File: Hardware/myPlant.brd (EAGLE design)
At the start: 141.4 x 16.8 mm, 42 parts, among them IC2 LMV358, Q2 MMBT2222A, SW1 KMR2, SW2 KMR2, U1 FSA3357, U2 NCP1402, U3 ALS-PT19, U6 SI7021, X1 ESP-12

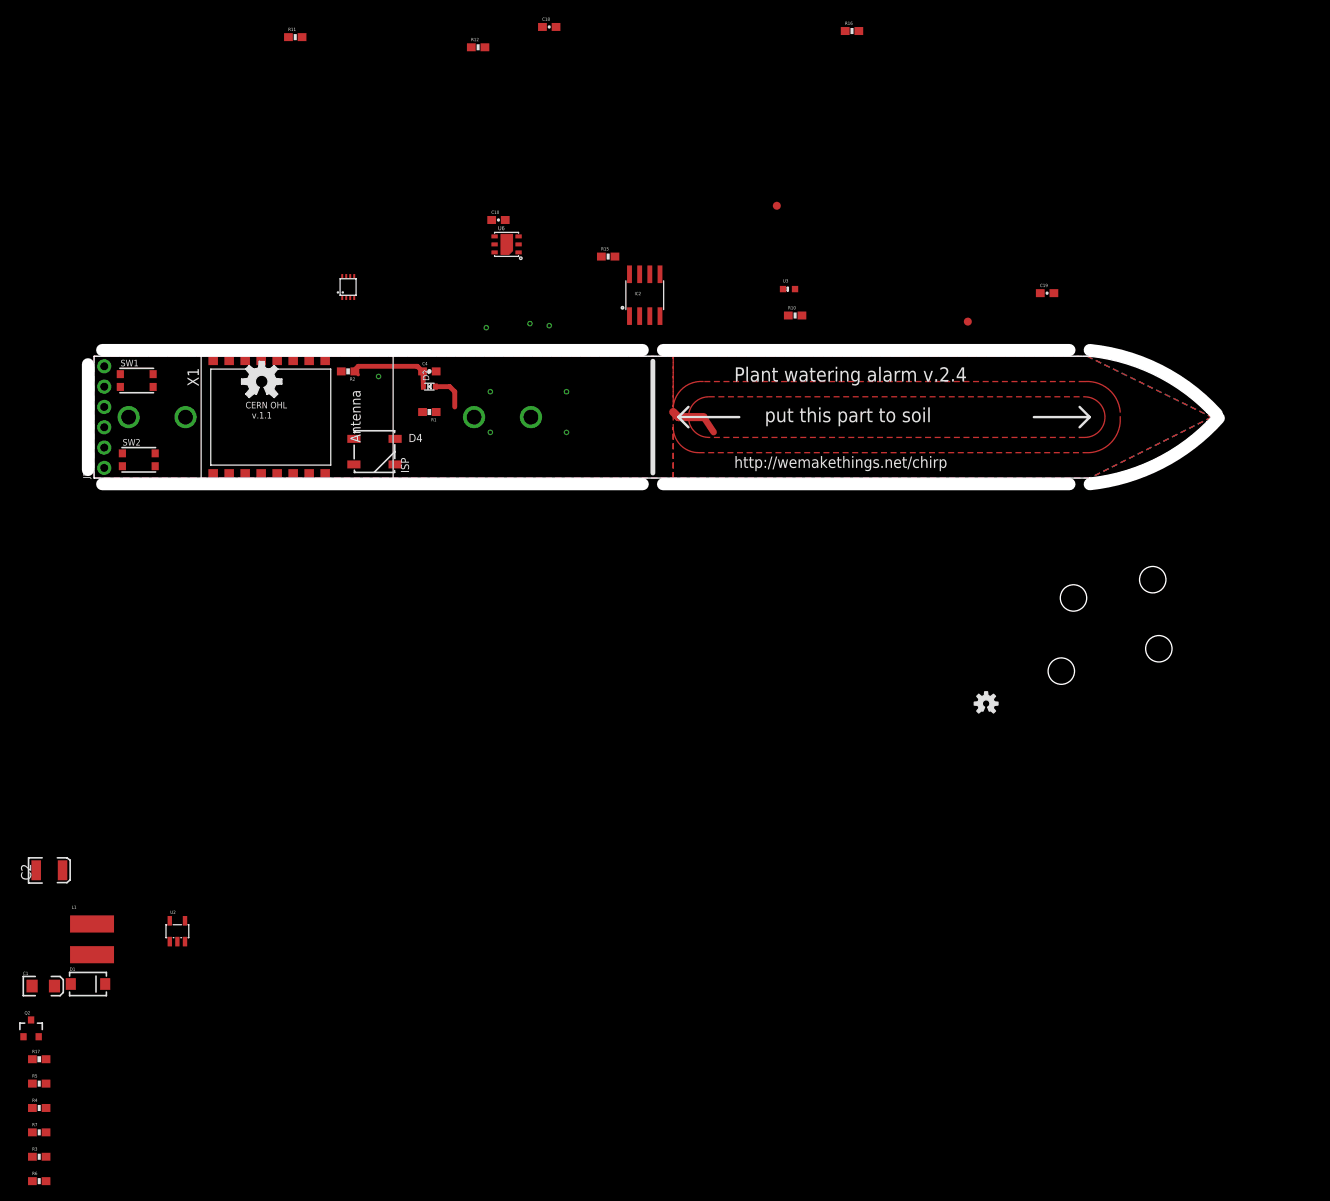
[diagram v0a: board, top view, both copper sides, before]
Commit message: Added load switch
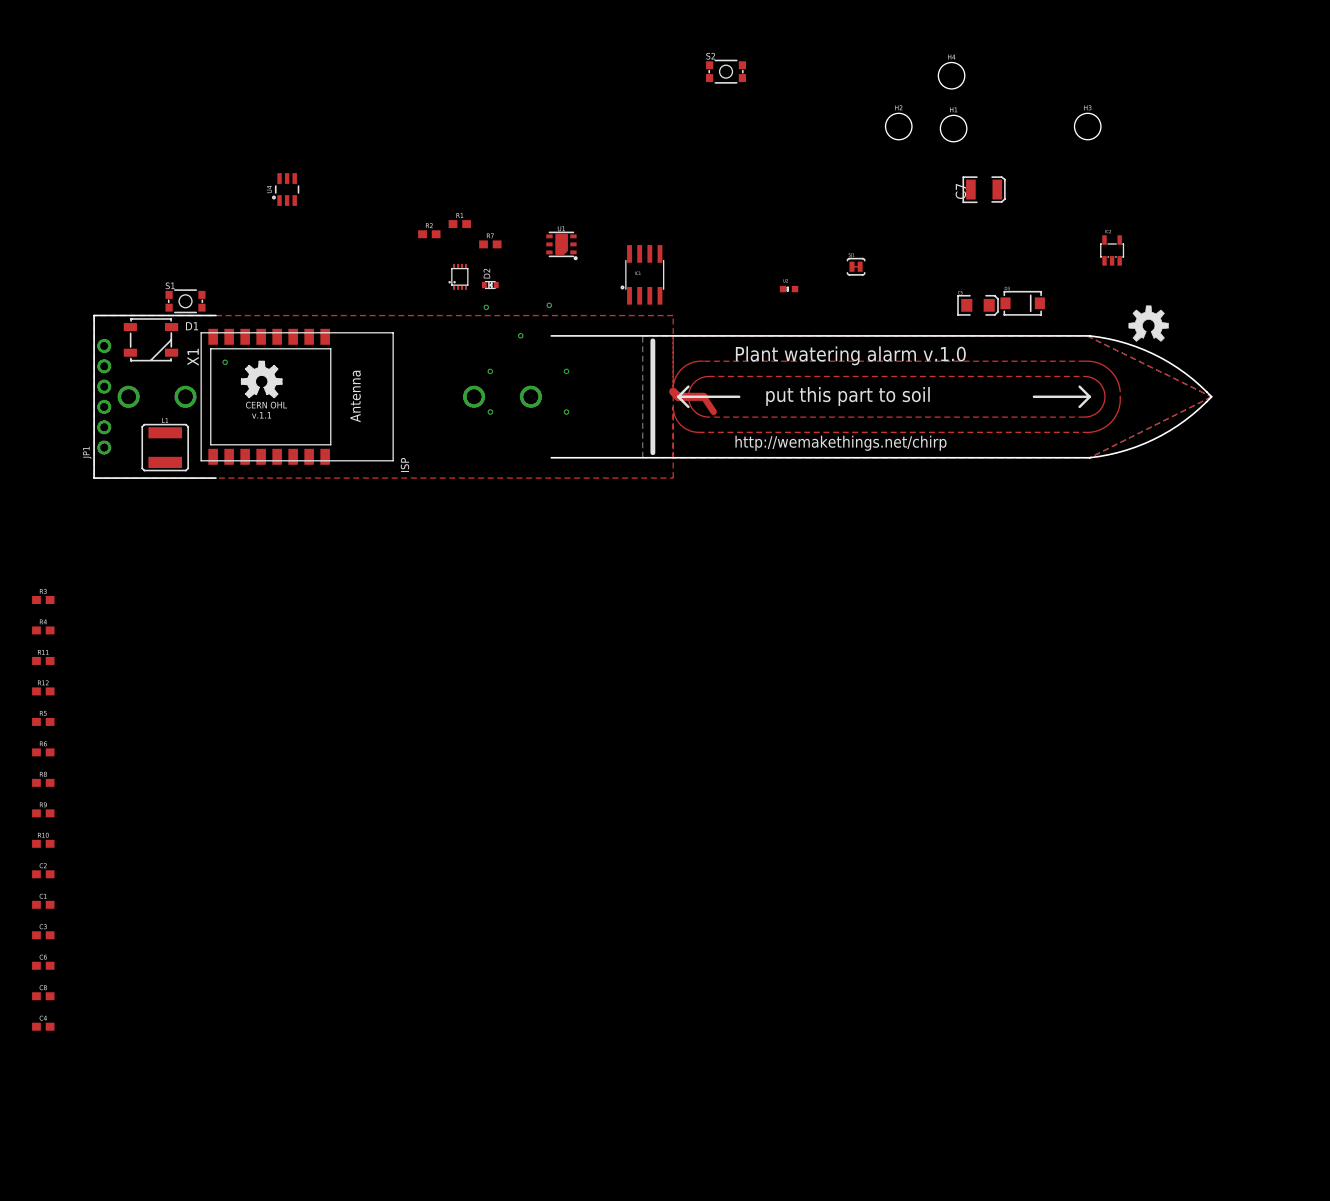
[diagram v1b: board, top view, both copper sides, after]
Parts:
- removed C10, C18, C19: 0.1uF, SparkFun-Capacitors:0603-CAP
- removed D4: WS2812, SparkFun-LED:WS2812B
- removed FID1, FID2: FIDUCIAL1X2, SparkFun-Aesthetics:FIDUCIAL-1X2
- removed LOGO2: OSHW-LOGOS, SparkFun-Aesthetics:OSHW-LOGO-S
- removed Q2: MMBT2222A, SparkFun-DiscreteSemi:SOT23-3@1
- removed R15, R16: 4.7K, SparkFun-Resistors:0603-RES
- removed R17: 10K, SparkFun-Resistors:0603-RES@1
- removed STANDOFF1, STANDOFF2, STANDOFF3, STANDOFF4: STAND-OFF, SparkFun-Electromechanical:STAND-OFF
- removed SW1, SW2: KMR2, microbuilder:BTN_KMR2_4.6X2.8
- removed U6: SI7021, SparkFun-Sensors:SI7021
- added C3, C6: 0.1uF, SparkFun-Capacitors:0603
- added C5: 10uF, SparkFun:EIA3216
- added C7: 68uF, SparkFun:EIA3528
- added C8: 1.0uF, SparkFun-Capacitors:0603
- added D3: MBRA140, SparkFun:SMA-DIODE
- added H1, H2, H3, H4: STAND-OFF, SparkFun-Hardware:STAND-OFF
- added IC1: LMV358, SparkFun-AnalogIC:SO08
- added LOGO1: OSHW-LOGOM, SparkFun-Aesthetics:OSHW-LOGO-M
- added R8, R9: 10k, SparkFun-Resistors:0603
- added S1: BTN-0, SparkFun-Electromechanical:TACTILE_SWITCH_SMD_4.6X2.8MM
- added S2: RESET, SparkFun-Electromechanical:TACTILE_SWITCH_SMD_4.6X2.8MM
- added SJ1: SLEEP, SparkFun-Passives:PAD-JUMPER-2-NC_BY_TRACE_YES_SILK
- added U4: TPS22860, alex:SOT23-6
- C1: value 10uF -> 0.1uF; device SparkFun:EIA3216 -> SparkFun-Capacitors:0603
- C2: value 68uF -> 1.0uF; device SparkFun:EIA3528 -> SparkFun-Capacitors:0603
- C4: value 1uF -> 0.1uF; device SparkFun:0603-CAP -> SparkFun-Capacitors:0603
- D1: value MBRA140 -> WS2812; device SparkFun:SMA-DIODE -> SparkFun-LED:WS2812B
- FRAME1: value FRAME-LEDGER -> FRAME-LETTER
- IC2: value LMV358 -> NCP1402; device SparkFun-AnalogIC:SO08 -> SparkFun:SOT23-5
- L1: value 47uH -> 47µH; device SparkFun:CR54 -> SparkFun-Coils:CR54
- R1: value 10K -> 510k; device SparkFun:0603-RES -> SparkFun-Resistors:0603
- R10, R12, R5, R6, R7: value 10K -> 10k; device SparkFun-Resistors:0603-RES -> SparkFun-Resistors:0603
- R11: value 22K -> 22k; device SparkFun-Resistors:0603-RES -> SparkFun-Resistors:0603
- R2: value 510K -> 10k; device SparkFun:0603-RES -> SparkFun-Resistors:0603
- R3, R4: value 10K -> 4.7k; device SparkFun-Resistors:0603-RES -> SparkFun-Resistors:0603
- U1: value FSA3357 -> SI7021; device alex:US8 -> SparkFun-Sensors:DFN-6-3X3-SI7021
- U2: value NCP1402 -> ALS-PT19; device SparkFun:SOT23-5 -> SparkFun-Sensors:ALS-PT19
- U3: value ALS-PT19 -> FSA3357; device SparkFun-Sensors:ALS-PT19 -> alex:US8
- moved R7 124.5 mm to (49.5, 29.2)
- moved R10 114.9 mm to (-6.35, -45.7)
- moved U2 110.8 mm to (86.9, 23.6)
- moved R12 97.1 mm to (-6.35, -26.7)
- moved C4 95.1 mm to (-6.35, -68.6)
- moved R11 84.1 mm to (-6.35, -22.9)
- moved D1 80.9 mm to (7.11, 17.3)
- moved R3 69.6 mm to (-6.35, -15.2)
- moved L1 62.1 mm to (8.89, 3.81)
- moved R4 59.7 mm to (-6.35, -19.1)
- moved IC2 58.7 mm to (127.3, 28.4)
- moved R6 53.6 mm to (-6.35, -34.3)
- moved R5 45.2 mm to (-6.35, -30.5)
- moved U3 41.2 mm to (45.7, 25.1)
- moved U1 27.2 mm to (58.4, 29.2)
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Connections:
- removed net CAPACITANCE_V: C4.1, D2.K, R2.1, U1.1
- removed net GPIO0: R5.1, SW2.B, SW2.B', X1.12
- removed net GPIO12: R17.1, X1.6
- removed net GPIO13: U1.6, X1.7
- removed net GPIO14: U1.5, X1.5
- removed net GPIO15: R1.2, R6.2, X1.10
- removed net GPIO2: D4.4, R7.1, X1.11
- removed net N$6: Q2.1, R17.2
- new net 0/BUTTON: R5.1, S1.3, S1.4, X1.12
- new net 12/S1: U3.6, X1.6
- new net 13/S2: U3.5, X1.7
- new net 14/PWR: U4.6, X1.5
- new net 15/CLK: R10.2, R2.2, X1.10
- new net 2/WS2812: D1.4, R8.1, X1.11
- new net CAPACITANCE: C2.1, D2.K, R1.2, U3.1
- new net GPIO16: SJ1.1, X1.4
- net 3.3V: now also C7.A, C8.1, D3.C, IC2.1, IC2.2, R6.2, R8.2, R9.2, U4.4, U4.5; no longer C2.A, D1.C, Q2.3, R3.2, R4.2, R7.2, U2.1, U2.2
- net 4/SDA: now also R3.1, U1.DATA; no longer R15.1, U6.DATA
- net 5/SCL: now also R4.1, U1.SCK; no longer R16.1, U6.SCK
- net ADC: now also IC1.6, IC1.7; no longer IC2.6, IC2.7
- net ADC-IN: now also IC1.3, U3.7; no longer IC2.3, U1.7
- net CH_PD: now also R9.1; no longer R3.1
- net GND: now also C1.2, C2.2, C3.2, C5.C, C6.2, C7.C, C8.2, D1.3, IC1.4, R1.1, R7.1, S1.1, S1.2, S2.1, S2.2, U1.GND, U3.4, U4.2; no longer C1.C, C10.2, C18.2, C19.2, C2.C, D4.3, R2.2, R6.1, SW1.A, SW1.A', SW2.A, SW2.A', U1.4, U2.4, U6.GND
- net LIGHT: now also R7.2, U2.E, U3.2; no longer R10.2, U1.2, U3.E
- net N$1: now also D3.A, IC2.5; no longer D1.A, U2.5
- net N$15: now also IC1.1, IC1.2; no longer IC2.1, IC2.2
- net N$18: now also IC1.5; no longer IC2.5
- net RAW: now also C5.A, U3.3; no longer C1.A, U1.3
- net RESET: now also R6.1, S2.3, S2.4, SJ1.2; no longer R4.1, SW1.B, SW1.B', X1.4
- net VCC: now also C1.1, C3.1, C4.1, C6.1, D1.1, IC1.8, R3.2, R4.2, U1.VDD, U2.C, U3.8, U4.1; no longer C10.1, C18.1, C19.1, D4.1, IC2.8, Q2.2, R15.2, R16.2, U1.8, U3.C, U6.VDD
- net V_CAP: now also R2.1; no longer R1.1
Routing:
- net CAPACITANCE_V: track 11.6 -> 0.00 mm
- net V_CAP: track 10.9 -> 6.33 mm
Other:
- board size 141.4 x 16.8 mm -> 139.7 x 20.3 mm
- board text added: "Plant watering alarm v.1.0"
- board text removed: "Plant watering alarm v.2.4"

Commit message: Done preliminary pcb placement
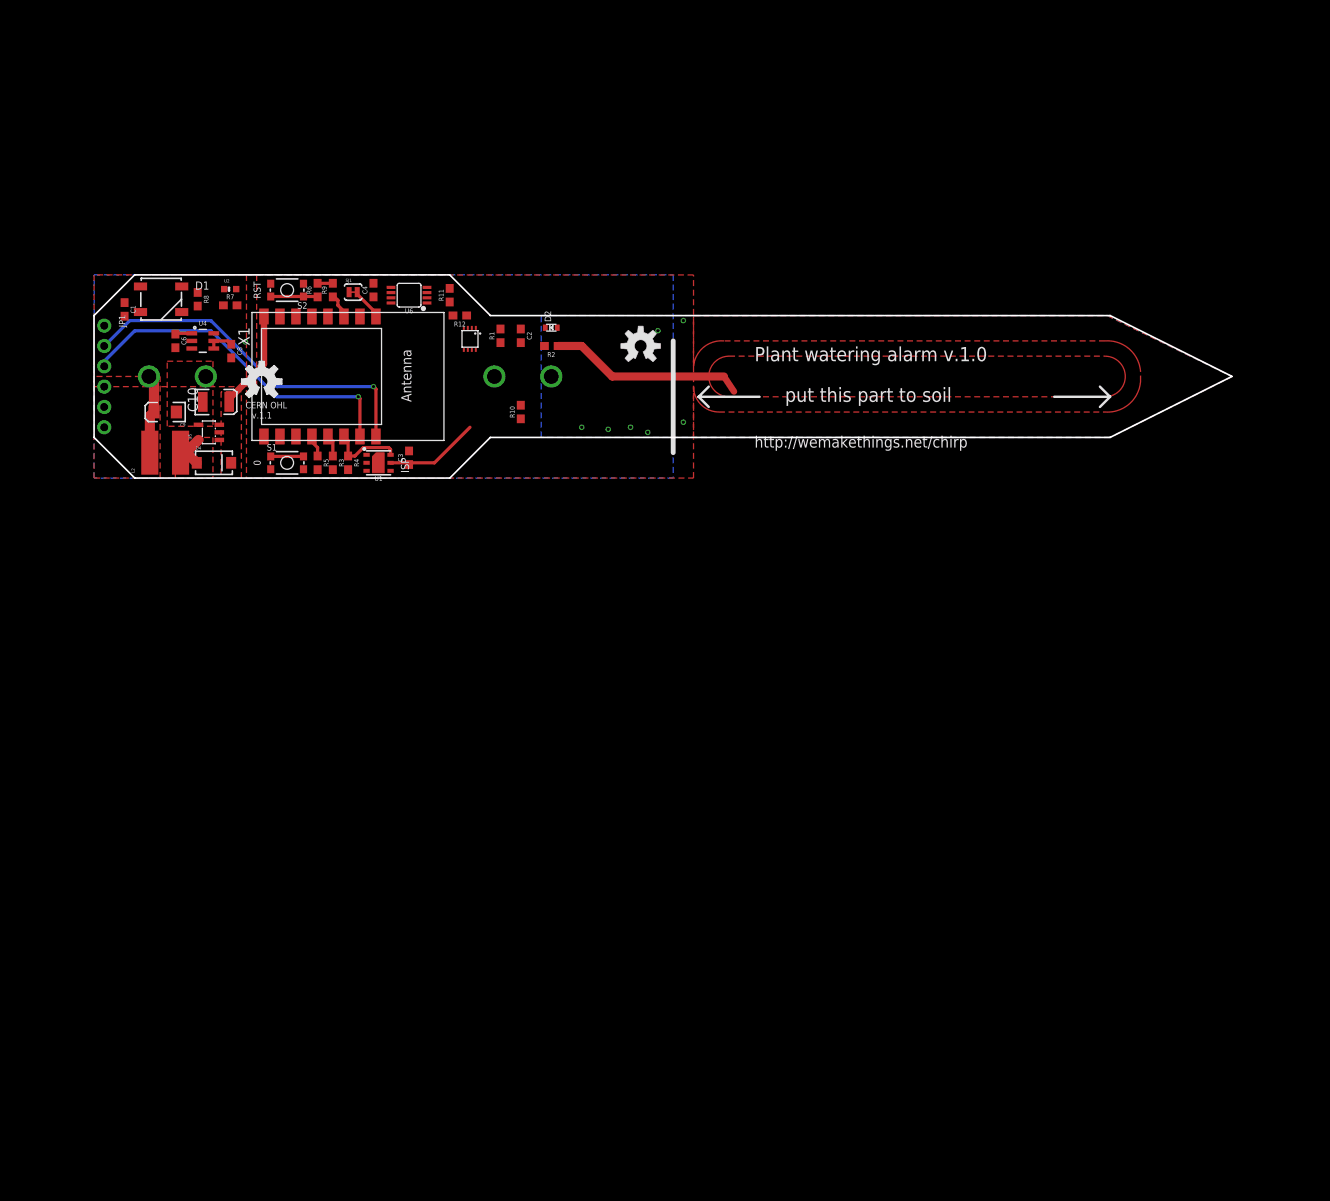
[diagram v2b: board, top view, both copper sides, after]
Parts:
- removed C5: 10uF, SparkFun:EIA3216
- removed C7: 68uF, SparkFun:EIA3528
- removed D3: MBRA140, SparkFun:SMA-DIODE
- removed H1, H2, H3, H4: STAND-OFF, SparkFun-Hardware:STAND-OFF
- removed IC1: LMV358, SparkFun-AnalogIC:SO08
- removed IC2: NCP1402, SparkFun:SOT23-5
- removed L1: 47µH, SparkFun-Coils:CR54
- added C10: 68uF, SparkFun:EIA3528
- added C9: 10uF, SparkFun:EIA3216
- added D4: MBRA140, SparkFun:SMA-DIODE
- added L2: 47uH, SparkFun:CR54
- added U5: NCP1402, SparkFun:SOT23-5
- added U6: (no value), SparkFun-IC-Amplifiers:MSOP8
- moved C4 100.9 mm to (34.9, 23.5), turned to 90 degrees
- moved C2 90.0 mm to (53.3, 17.8), turned to 270 degrees
- moved C8 84.0 mm to (17.1, 15.9), turned to 270 degrees
- moved R10 80.5 mm to (53.3, 8.26), turned to 90 degrees
- moved C6 79.8 mm to (10.2, 17.1), turned to 270 degrees
- moved C3 75.2 mm to (39.4, 2.54), turned to 90 degrees
- moved C1 75.1 mm to (3.81, 21.1), turned to 270 degrees
- moved R9 74.8 mm to (29.8, 23.5), turned to 90 degrees
- moved R12 70.1 mm to (45.7, 20.3), turned to 180 degrees
- moved U2 69.8 mm to (17.0, 23.6)
- moved R11 68.3 mm to (44.5, 22.9), turned to 90 degrees
- moved R6 67.2 mm to (27.9, 23.5), turned to 90 degrees
- moved LOGO1 63.6 mm to (68.3, 16.5)
- moved R8 63.5 mm to (13.0, 22.4), turned to 270 degrees
- moved SJ1 62.9 mm to (32.4, 23.2)
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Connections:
- removed net N$1: D3.A, IC2.5, L1.P$2
- removed net RAW: BAT1.PWR@1, C5.A, L1.P$1, U3.3
- new net N$3: D4.A, L2.P$2, U5.5
- new net VBAT: BAT1.PWR@1, C9.A, L2.P$1, U3.3
- net 3.3V: now also C10.A, D4.C, U5.1, U5.2; no longer C7.A, D3.C, IC2.1, IC2.2
- net ADC: now also U6.6, U6.7; no longer IC1.6, IC1.7
- net ADC-IN: now also U6.3; no longer IC1.3
- net GND: now also C10.C, C9.C, U5.4, U6.4; no longer C5.C, C7.C, IC1.4, IC2.4
- net N$15: now also U6.1, U6.2; no longer IC1.1, IC1.2
- net N$18: now also U6.5; no longer IC1.5
- net VCC: now also U6.8; no longer IC1.8
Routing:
- net TXD: track 0.00 -> 44.7 mm, vias 0 -> 1
- net RXD: track 0.00 -> 42.4 mm, vias 0 -> 1
- net V_CAP: track 6.33 -> 24.6 mm
- net 3.3V: track 0.00 -> 17.7 mm
- net VCC: track 0.00 -> 14.2 mm
- net VBAT: track 0.00 -> 10.0 mm
- net RESET: track 0.00 -> 9.89 mm
- net 5/SCL: track 0.00 -> 9.18 mm
- net 0/BUTTON: track 0.00 -> 6.84 mm
- net N$3: track 0.00 -> 5.45 mm
- net CH_PD: track 0.00 -> 3.15 mm
- net 4/SDA: track 0.00 -> 2.70 mm
- added copper zone on layer 1, net 3.3V
- added copper zone on layer 1, net N$3
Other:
- board size 139.7 x 20.3 mm -> 142.2 x 25.4 mm
- board text added: "0"
- board text added: "RST"

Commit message: Complete PCB layout
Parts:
- removed LOGO1: OSHW-LOGOM, SparkFun-Aesthetics:OSHW-LOGO-M
- moved R3 19.1 mm to (48.9, 1.40), turned to 0 degrees
- moved R4 18.5 mm to (48.9, 8.76), turned to 0 degrees
- moved U1 13.7 mm to (48.9, 5.08), turned to 270 degrees
- moved C3 13.0 mm to (52.1, 5.08)
- moved R10 6.74 mm to (53.1, 15.0), turned to 0 degrees
- moved U3 6.45 mm to (50.4, 22.9), turned to 90 degrees
- moved R11 1.42 mm to (45.7, 22.2), turned to 180 degrees
- moved R1 1.27 mm to (52.1, 17.8)
- moved U6 1.27 mm to (40.6, 22.9)
- moved S1 0.76 mm to (23.4, 1.91)
- moved S2 0.76 mm to (23.4, 23.5)
- moved R8 0.64 mm to (13.0, 21.7)
- moved C1 0.63 mm to (3.81, 21.7)
- moved C2 0.63 mm to (54.0, 17.8)
- moved C4 0.51 mm to (35.4, 23.5), turned to 270 degrees
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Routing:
- net VBAT: track 10.0 -> 97.8 mm, vias 0 -> 2
- net VCC: track 14.2 -> 100.2 mm, vias 0 -> 2
- net LIGHT: track 0.00 -> 66.3 mm, vias 0 -> 2
- net 3.3V: track 17.7 -> 71.7 mm, vias 0 -> 2
- net 15/CLK: track 0.00 -> 48.7 mm, vias 0 -> 2
- net 13/S2: track 0.00 -> 32.3 mm, vias 0 -> 2
- net 12/S1: track 0.00 -> 31.0 mm, vias 0 -> 2
- net 2/WS2812: track 0.00 -> 26.7 mm, vias 0 -> 2
- net 4/SDA: track 2.70 -> 23.8 mm
- net 5/SCL: track 9.18 -> 24.6 mm
- net 14/PWR: track 0.00 -> 14.9 mm, vias 0 -> 2
- net N$18: track 0.00 -> 14.7 mm, vias 0 -> 2
- net RESET: track 9.89 -> 22.4 mm, vias 0 -> 2
- net V_CAP: track 24.6 -> 37.1 mm
- net ADC: track 0.00 -> 10.4 mm
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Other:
- board size 142.2 x 25.4 mm -> 152.4 x 25.4 mm
- board text added: "myPlant"
- board text removed: "CERN OHL"
- board text removed: "ISP"
- board text removed: "Plant watering alarm v.1.0"
- board text removed: "chirp!"
- board text removed: "http://wemakethings.net/chirp"
- board text removed: "v.1.1"
